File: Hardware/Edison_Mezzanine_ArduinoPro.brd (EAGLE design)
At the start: 30.5 x 53.3 mm, 37 parts, among them U1 MIC5205-3.3V (150mA), U2 EDISON_CONNECTOR_FULLMOUNTING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, U3 EDISON_CONNECTOR_FULLHEADER, U4 ATMEGA328, Y1 8MHZ

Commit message: expanding out connector, matching it to Arduino Pro
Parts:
- added JP4, JP5: M021X02_NO_SILK, SparkFun-Connectors:1X02_NO_SILK
- JP2, JP3: value M12PTH -> M121X12_NO_SILK_KIT; device SparkFun-Connectors:1X12 -> SparkFun-Connectors:1X12_NO_SILK_KIT
- moved JP2 8.89 mm to (1.27, 61.0)
- moved R6 3.81 mm to (2.54, 11.4)
- moved R11 2.54 mm to (2.54, 7.62)
- moved D3 2.54 mm to (2.54, 10.2)
- moved JP1 2.54 mm to (1.97, 27.9)
- moved LED1 1.27 mm to (2.54, 6.35)
- moved JP3 1.27 mm to (1.27, 45.7)
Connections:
- net A4: now also JP4.1; no longer JP2.3
- net A5: now also JP4.2; no longer JP2.4
- net A6: now also JP5.1
- net A7: now also JP5.2
- net ARD_RX: now also JP3.2; no longer JP3.3
- net ARD_TX: now also JP3.1; no longer JP3.4
- net GND: now also JP2.2, JP3.4; no longer JP2.1
- net RESET: now also JP2.3, JP3.3; no longer JP3.2
- net VCC: now also JP2.4; no longer JP2.2
- net VIN: now also JP2.1; no longer JP3.1
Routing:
- net A6: track 0.00 -> 27.2 mm, vias 0 -> 2
- net A7: track 0.00 -> 25.8 mm, vias 0 -> 2
- net RESET: track 19.3 -> 38.5 mm
- net VIN: track 65.5 -> 83.2 mm
- net SCK: track 46.9 -> 63.1 mm
- net A0: track 19.5 -> 31.7 mm
- net A3: track 22.4 -> 32.7 mm
- net A2: track 22.2 -> 32.1 mm
- net A1: track 18.8 -> 28.5 mm
- net MISO: track 20.5 -> 29.7 mm
- net MOSI: track 22.8 -> 31.7 mm
- net D10: track 24.8 -> 33.7 mm
- net A5: track 24.1 -> 32.1 mm, vias 2 -> 3
- net A4: track 22.5 -> 29.1 mm, vias 0 -> 3
- net VCC: track 95.0 -> 100.6 mm
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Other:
- board size 30.5 x 53.3 mm -> 30.5 x 62.2 mm
- board text added: "10"
- board text added: "11"
- board text added: "12"
- board text added: "13"
- board text added: "2"
- board text added: "3"
- board text added: "4"
- board text added: "5"
- board text added: "6"
- board text added: "7"
- board text added: "8"
- board text added: "9"
- board text added: "A6"
- board text added: "A7"
- board text added: "Arduino"
- board text removed: "Arduino Stack"
- board text removed: "Connectors Go Here"
- board text removed: "D10"
- board text removed: "D11"
- board text removed: "D12"
- board text removed: "D2"
- board text removed: "D3"
- board text removed: "D4"
- board text removed: "D5"
- board text removed: "D6"
- board text removed: "D7"
- board text removed: "D8"
- board text removed: "D9"
- board text removed: "LED's and selector switches go here"
- board text removed: "Max Board Length"
- board text removed: "Nothing goes here... I mean it."

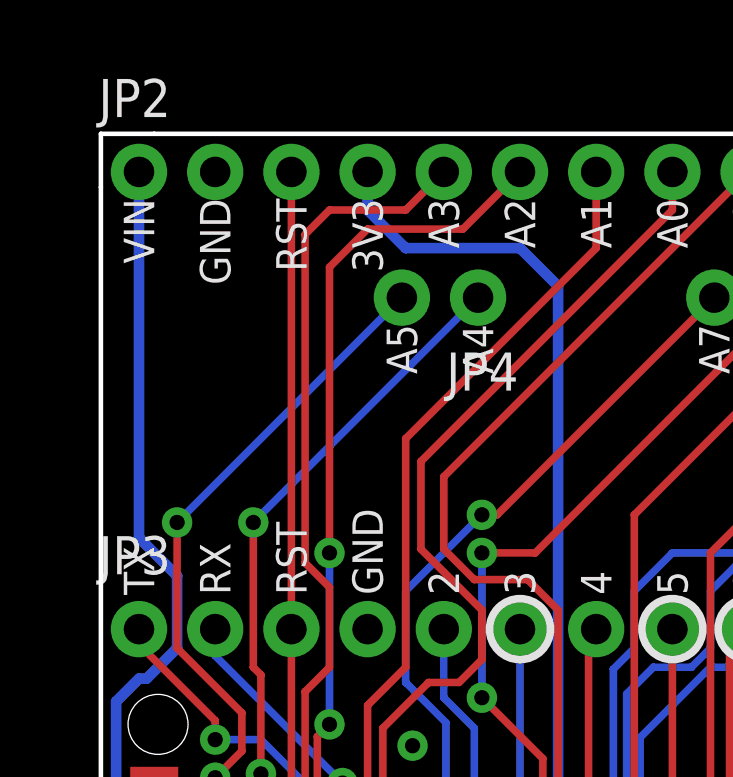
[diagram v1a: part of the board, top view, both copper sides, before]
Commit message: fixing 12-pin connectors - using NO_SILK part now
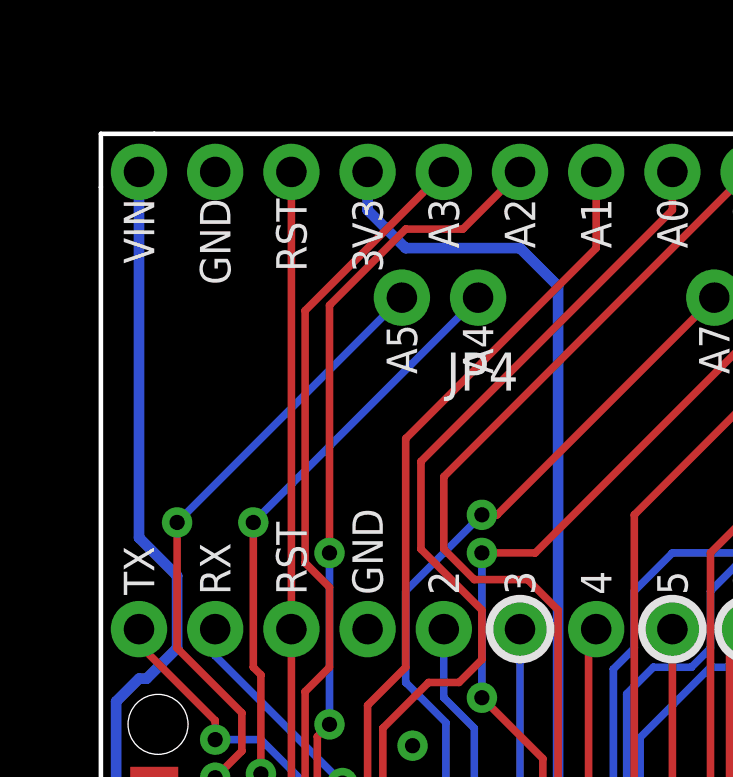
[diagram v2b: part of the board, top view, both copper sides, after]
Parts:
- JP2, JP3: value M121X12_NO_SILK_KIT -> M12NO_SILK; device SparkFun-Connectors:1X12_NO_SILK_KIT -> SparkFun-Connectors:1X12_NO_SILK
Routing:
- net A3: track 32.7 -> 31.2 mm
- net A2: track 32.1 -> 31.4 mm
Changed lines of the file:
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@@
 <?xml version="1.0" encoding="utf-8"?>
 <!DOCTYPE eagle SYSTEM "eagle.dtd">
-<eagle version="6.5.0">
+<eagle version="7.1.0">
 <drawing>
 <settings>
@@
 <pass name="Default">
 <param name="RoutingGrid" value="50mil"/>
+<param name="AutoGrid" value="1"/>
+<param name="Efforts" value="0"/>
+<param name="TopRouterVariant" value="1"/>
 <param name="tpViaShape" value="round"/>
 <param name="PrefDir.1" value="|"/>
@@
 <element name="C4" library="SparkFun" package="0603-CAP" value="0.1uF" x="8.89" y="10.795" rot="R180"/>
 <element name="C5" library="SparkFun" package="0603-CAP" value="0.1uF" x="13.97" y="10.795"/>
-<element name="JP2" library="SparkFun-Connectors" package="1X12_NO_SILK_KIT" value="M121X12_NO_SILK_KIT" x="1.27" y="60.96"/>
-<element name="JP3" library="SparkFun-Connectors" package="1X12_NO_SILK_KIT" value="M121X12_NO_SILK_KIT" x="1.27" y="45.72"/>
+<element name="JP2" library="SparkFun-Connectors" package="1X12_NO_SILK" value="M12NO_SILK" x="1.27" y="60.96"/>
+<element name="JP3" library="SparkFun-Connectors" package="1X12_NO_SILK" value="M12NO_SILK" x="1.27" y="45.72"/>
 <element name="JP4" library="SparkFun-Connectors" package="1X02_NO_SILK" value="M021X02_NO_SILK" x="12.573" y="56.769" rot="R180"/>
 <element name="JP5" library="SparkFun-Connectors" package="1X02_NO_SILK" value="M021X02_NO_SILK" x="22.987" y="56.769" rot="R180"/>
@@
 <contactref element="JP2" pad="5"/>
 <wire x1="7.62" y1="44.45" x2="7.62" y2="47.117" width="0.254" layer="1"/>
-<wire x1="6.8072" y1="47.9298" x2="6.8072" y2="58.8772" width="0.254" layer="1"/>
+<wire x1="6.8072" y1="47.9298" x2="6.8072" y2="56.3372" width="0.254" layer="1"/>
 <wire x1="6.8072" y1="47.9298" x2="7.62" y2="47.117" width="0.254" layer="1"/>
 <wire x1="6.8072" y1="43.6372" x2="7.62" y2="44.45" width="0.254" layer="1"/>
-<wire x1="6.8072" y1="58.8772" x2="7.62" y2="59.69" width="0.254" layer="1"/>
-<wire x1="7.62" y1="59.69" x2="10.16" y2="59.69" width="0.254" layer="1"/>
-<wire x1="10.16" y1="59.69" x2="11.43" y2="60.96" width="0.254" layer="1"/>
+<wire x1="6.8072" y1="56.3372" x2="11.43" y2="60.96" width="0.254" layer="1"/>
 </signal>
 <signal name="A2">
@@
 <wire x1="7.62" y1="42.545" x2="7.62" y2="48.26" width="0.254" layer="16"/>
 <via x="7.62" y="48.26" extent="1-16" drill="0.508"/>
-<wire x1="7.62" y1="48.26" x2="7.62" y2="57.785" width="0.254" layer="1"/>
-<wire x1="7.62" y1="57.785" x2="8.89" y2="59.055" width="0.254" layer="1"/>
-<wire x1="8.89" y1="59.055" x2="12.065" y2="59.055" width="0.254" layer="1"/>
+<wire x1="7.62" y1="48.26" x2="7.62" y2="56.515" width="0.254" layer="1"/>
+<wire x1="7.62" y1="56.515" x2="10.16" y2="59.055" width="0.254" layer="1"/>
+<wire x1="10.16" y1="59.055" x2="12.065" y2="59.055" width="0.254" layer="1"/>
 <wire x1="12.065" y1="59.055" x2="13.97" y2="60.96" width="0.254" layer="1"/>
 </signal>
